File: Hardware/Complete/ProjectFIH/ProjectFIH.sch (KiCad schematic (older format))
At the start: 84 parts, among them J1 Conn_01x02_Male, J10 Payload LED, J2 Power, J3 Power LED, J4 MCU Fail LED, J5 Heater LED, J6 Heater, J7 UART, J8 AVR-ISP-10, J9 Payload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

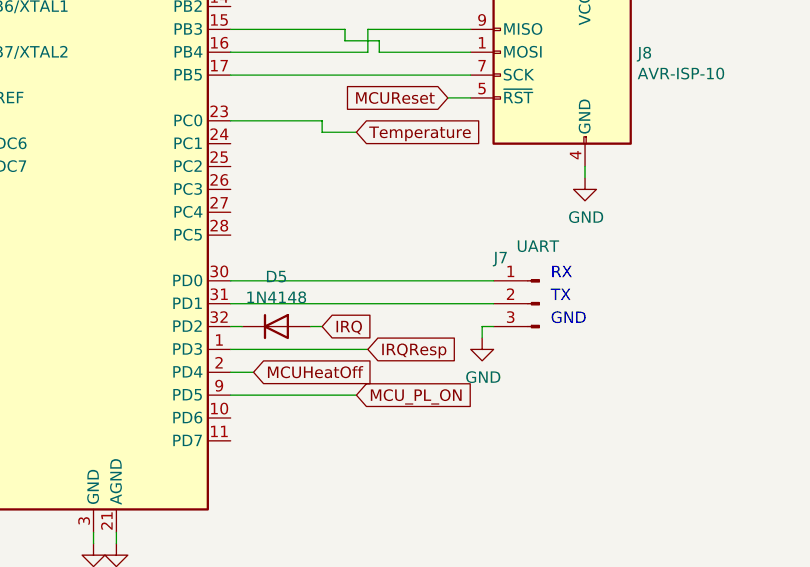
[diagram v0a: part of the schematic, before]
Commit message: MCU coupled with hardware watchdog
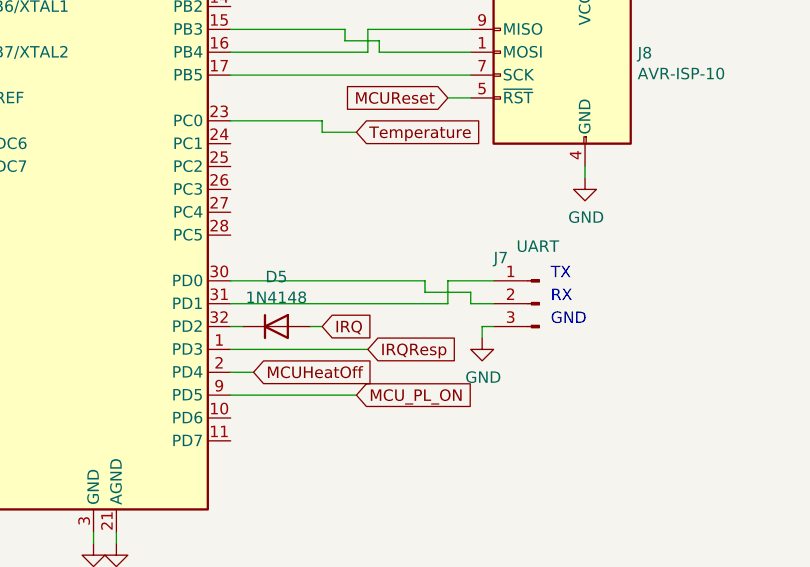
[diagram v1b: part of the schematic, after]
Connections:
- net at U8.30 (PD0): now also J7.2 (Pin_2); no longer J7.1 (Pin_1)
- net at U8.31 (PD1): now also J7.1 (Pin_1); no longer J7.2 (Pin_2)
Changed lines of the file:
@@
 	-1   0    0    -1
 $EndComp
-Wire Wire Line
-	12300 6450 11150 6450
-Wire Wire Line
-	12300 6550 11150 6550
 $Comp
 L power:GND #PWR059
@@
 Wire Wire Line
 	12250 6650 12250 6700
+Text Notes 12550 6550 0    50   ~ 0
+RX
 Text Notes 12550 6450 0    50   ~ 0
-RX
-Text Notes 12550 6550 0    50   ~ 0
 TX
 Text Notes 12550 6650 0    50   ~ 0
@@
 	8200 2400 8200 2550
 Connection ~ 8200 2550
+Wire Wire Line
+	11150 6550 12100 6550
+Wire Wire Line
+	12100 6550 12100 6450
+Wire Wire Line
+	12100 6450 12300 6450
+Wire Wire Line
+	12300 6550 12200 6550
+Wire Wire Line
+	12200 6550 12200 6500
+Wire Wire Line
+	12200 6500 12000 6500
+Wire Wire Line
+	12000 6500 12000 6450
+Wire Wire Line
+	12000 6450 11150 6450
 $EndSCHEMATC

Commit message: Small corrections after laying IRL parts out
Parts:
- C13, C14, C9: footprint Capacitor_THT:CP_Radial_D12.5mm_P7.50mm -> Capacitor_THT:CP_Radial_D12.5mm_P5.00mm
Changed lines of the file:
@@
 F 0 "C13" H 8850 1500 50  0000 L CNN
 F 1 "1000uF x 48V" H 8550 1300 50  0000 L CNN
-F 2 "Capacitor_THT:CP_Radial_D12.5mm_P7.50mm" H 8888 1250 50  0001 C CNN
+F 2 "Capacitor_THT:CP_Radial_D12.5mm_P5.00mm" H 8888 1250 50  0001 C CNN
 F 3 "~" H 8850 1400 50  0001 C CNN
 	1    8850 1400
@@
 F 0 "C14" H 8850 3100 50  0000 L CNN
 F 1 "1000uF x 48V" H 8550 2900 50  0000 L CNN
-F 2 "Capacitor_THT:CP_Radial_D12.5mm_P7.50mm" H 8888 2850 50  0001 C CNN
+F 2 "Capacitor_THT:CP_Radial_D12.5mm_P5.00mm" H 8888 2850 50  0001 C CNN
 F 3 "~" H 8850 3000 50  0001 C CNN
 	1    8850 3000
@@
 F 0 "C9" H 4218 9596 50  0000 L CNN
 F 1 "1000uFx50V" H 4218 9505 50  0000 L CNN
-F 2 "Capacitor_THT:CP_Radial_D12.5mm_P7.50mm" H 4138 9400 50  0001 C CNN
+F 2 "Capacitor_THT:CP_Radial_D12.5mm_P5.00mm" H 4138 9400 50  0001 C CNN
 F 3 "~" H 4100 9550 50  0001 C CNN
 	1    4100 9550

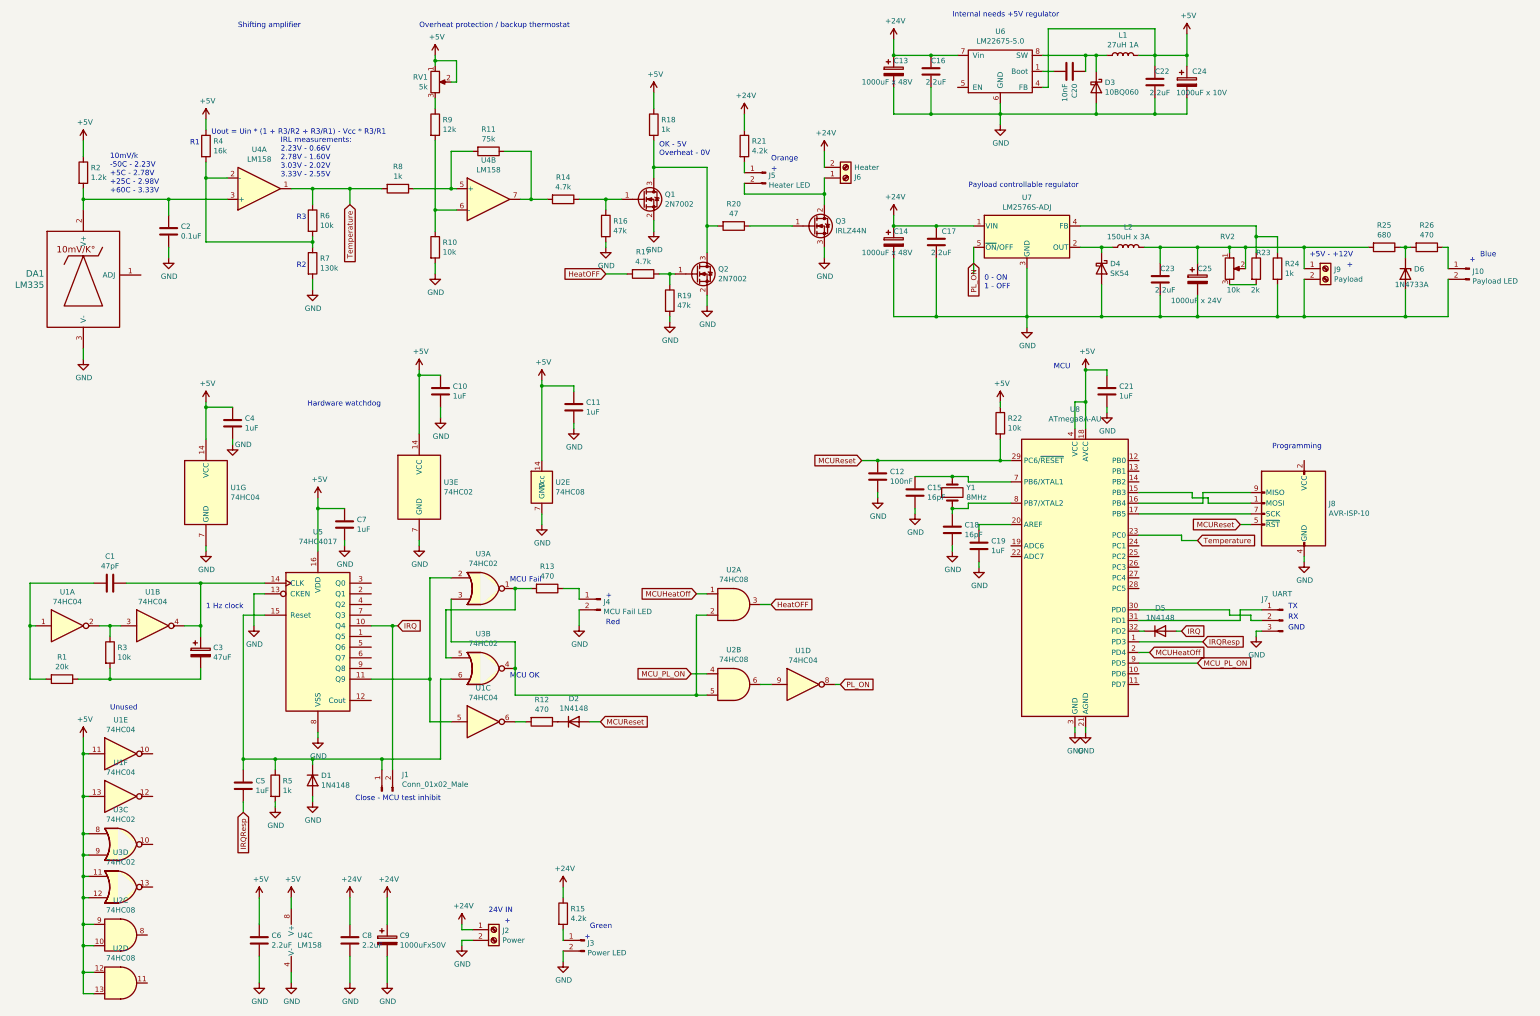
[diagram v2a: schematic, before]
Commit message: Flipped some (but not all needed) parts to other side
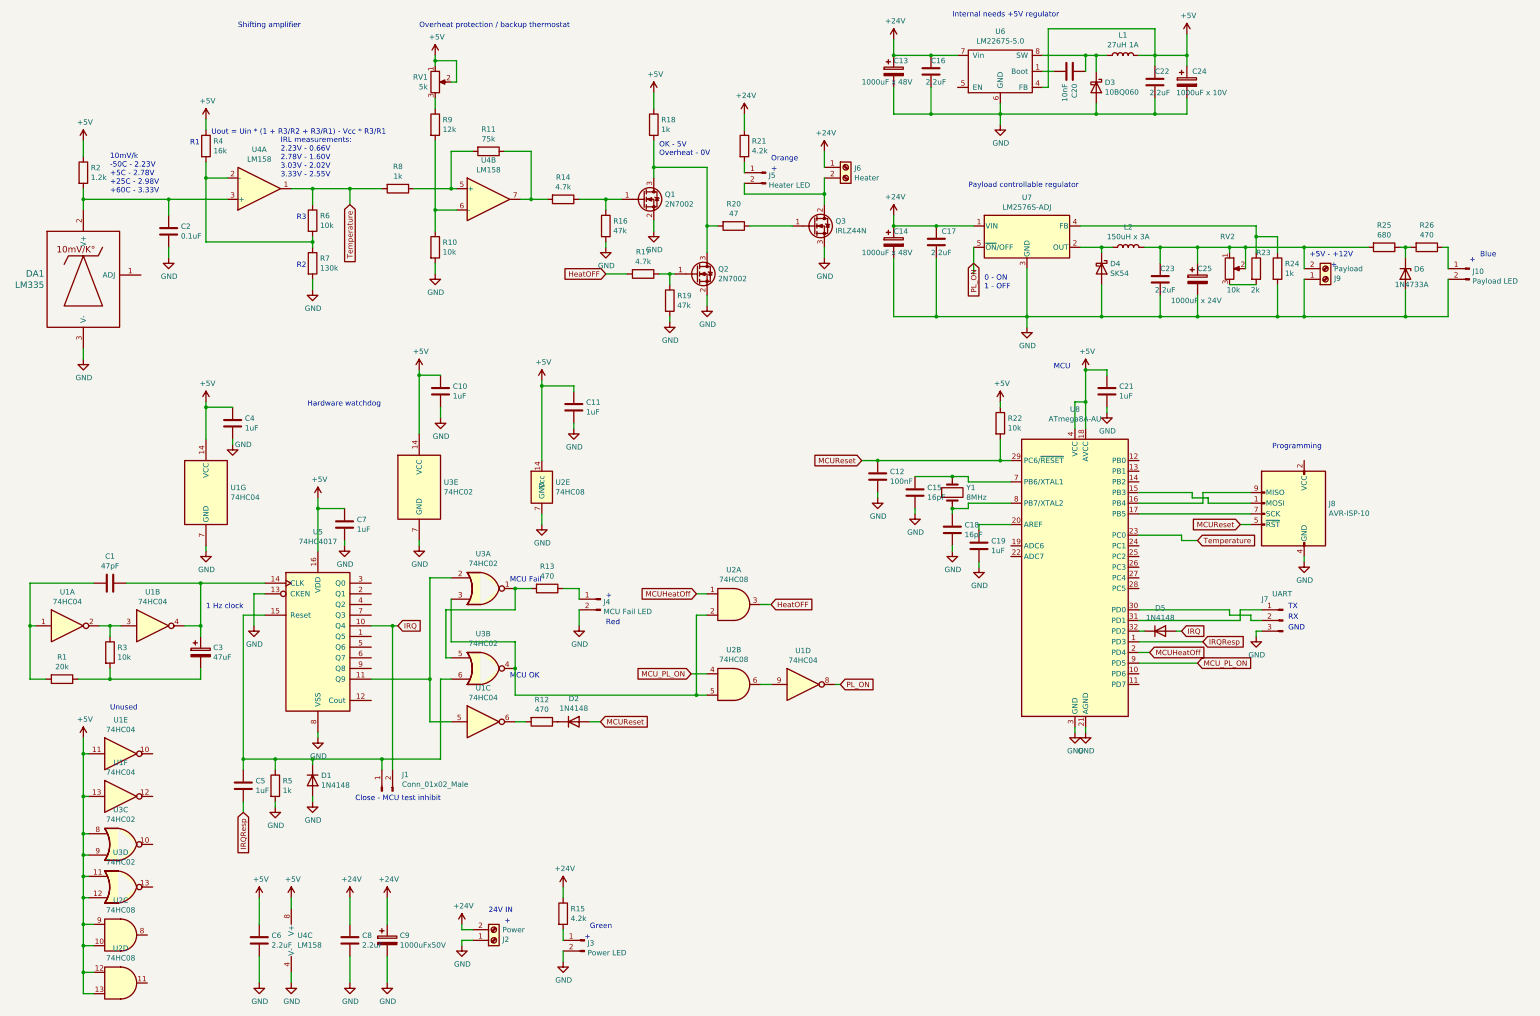
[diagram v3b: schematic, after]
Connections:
- net +24V: now also J2.2 (Pin_2), J6.1 (Pin_1); no longer J2.1 (Pin_1), J6.2 (Pin_2)
- net GND: now also J2.1 (Pin_1), J9.1 (Pin_1); no longer J2.2 (Pin_2), J9.2 (Pin_2)
- net at J5.2 (Pin_2), Q3.2 (D): now also J6.2 (Pin_2); no longer J6.1 (Pin_1)
- net at C23.1, C25.1, L2.2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: now also J9.2 (Pin_2); no longer J9.1 (Pin_1)
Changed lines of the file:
@@
 L Connector:Screw_Terminal_01x02 J6
 U 1 1 5F039ABC
-P 8400 2400
-F 0 "J6" H 8480 2392 50  0000 L CNN
-F 1 "Heater" H 8480 2301 50  0000 L CNN
-F 2 "TerminalBlock:TerminalBlock_Altech_AK300-2_P5.00mm" H 8400 2400 50  0001 C CNN
-F 3 "~" H 8400 2400 50  0001 C CNN
-	1    8400 2400
-	1    0    0    1
+P 8400 2300
+F 0 "J6" H 8480 2292 50  0000 L CNN
+F 1 "Heater" H 8480 2201 50  0000 L CNN
+F 2 "TerminalBlock:TerminalBlock_Altech_AK300-2_P5.00mm" H 8400 2300 50  0001 C CNN
+F 3 "~" H 8400 2300 50  0001 C CNN
+	1    8400 2300
+	1    0    0    -1
 $EndComp
 $Comp
@@
 L Connector:Screw_Terminal_01x02 J9
 U 1 1 5F15006B
-P 12900 3250
-F 0 "J9" H 12980 3242 50  0000 L CNN
-F 1 "Payload" H 12980 3151 50  0000 L CNN
-F 2 "TerminalBlock:TerminalBlock_Altech_AK300-2_P5.00mm" H 12900 3250 50  0001 C CNN
-F 3 "~" H 12900 3250 50  0001 C CNN
-	1    12900 3250
-	1    0    0    -1
+P 12900 3350
+F 0 "J9" H 12980 3342 50  0000 L CNN
+F 1 "Payload" H 12980 3251 50  0000 L CNN
+F 2 "TerminalBlock:TerminalBlock_Altech_AK300-2_P5.00mm" H 12900 3350 50  0001 C CNN
+F 3 "~" H 12900 3350 50  0001 C CNN
+	1    12900 3350
+	1    0    0    1
 $EndComp
 Wire Wire Line
@@
 L Connector:Screw_Terminal_01x02 J2
 U 1 1 5F880536
-P 5100 9450
-F 0 "J2" H 5180 9442 50  0000 L CNN
-F 1 "Power" H 5180 9351 50  0000 L CNN
-F 2 "TerminalBlock:TerminalBlock_Altech_AK300-2_P5.00mm" H 5100 9450 50  0001 C CNN
-F 3 "~" H 5100 9450 50  0001 C CNN
-	1    5100 9450
-	1    0    0    -1
+P 5100 9550
+F 0 "J2" H 5180 9542 50  0000 L CNN
+F 1 "Power" H 5180 9451 50  0000 L CNN
+F 2 "TerminalBlock:TerminalBlock_Altech_AK300-2_P5.00mm" H 5100 9550 50  0001 C CNN
+F 3 "~" H 5100 9550 50  0001 C CNN
+	1    5100 9550
+	1    0    0    1
 $EndComp
 $Comp
@@
 Text Notes 5200 9400 0    50   ~ 0
 +
-Text Notes 13100 3250 0    50   ~ 0
+Text Notes 12950 3250 0    50   ~ 0
 +
 $Comp

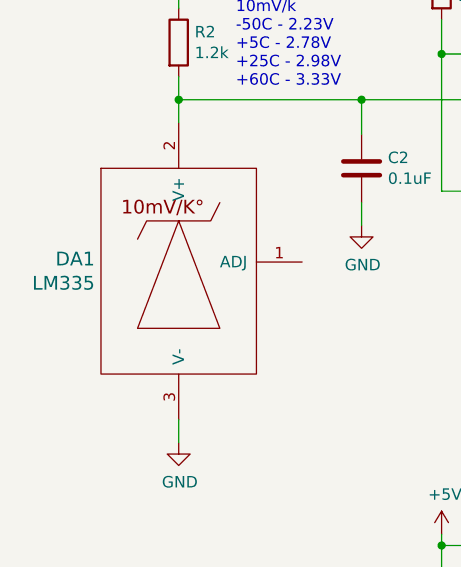
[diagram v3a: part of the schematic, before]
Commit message: LM335 -> LM135
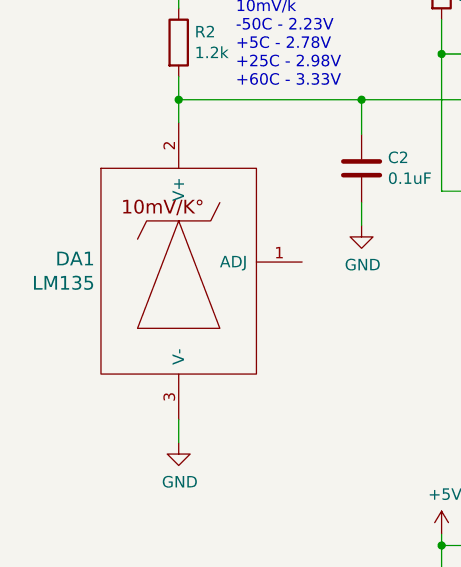
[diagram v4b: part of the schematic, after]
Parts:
- DA1: value LM335 -> LM135
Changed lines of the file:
@@
 P 1250 2900
 F 0 "DA1" H 883 2503 60  0000 R CNN
-F 1 "LM335" H 883 2397 60  0000 R CNN
+F 1 "LM135" H 883 2397 60  0000 R CNN
 F 2 "Package_TO_SOT_THT:TO-92" H 1240 2910 60  0001 C CNN
 F 3 "" H 1240 2910 60  0000 C CNN

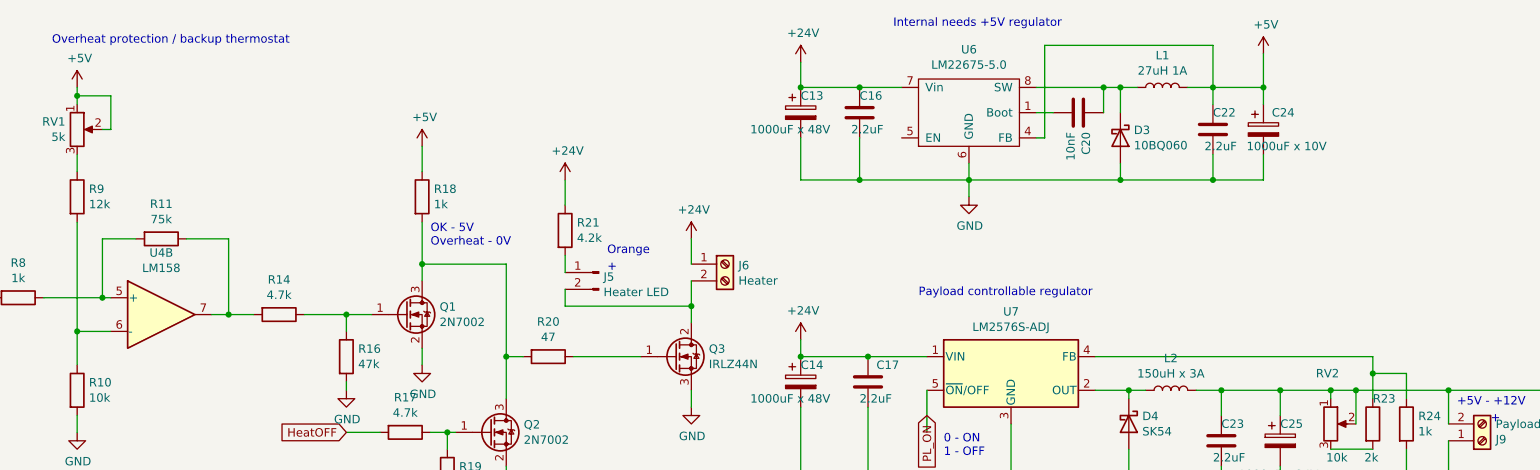
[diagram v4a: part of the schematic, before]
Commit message: Small comments on schematic
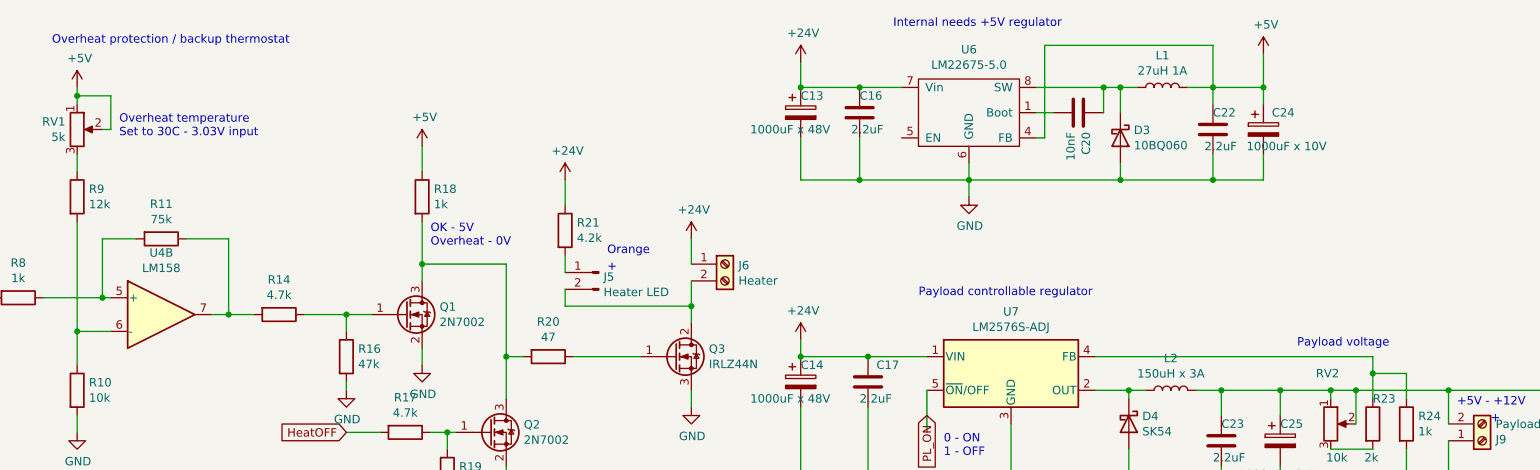
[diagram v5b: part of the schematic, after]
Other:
- note added: "Overheat temperature\nSet to 30C - 3.03V input"
- note added: "Payload voltage"
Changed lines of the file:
@@
 Wire Wire Line
 	12000 6450 11150 6450
+Text Notes 11800 2800 0    50   ~ 0
+Payload voltage
+Text Notes 4800 1550 0    50   ~ 0
+Overheat temperature\nSet to 30C - 3.03V input
 $EndSCHEMATC

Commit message: Small corrections
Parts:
- added R27: 470, Resistor_SMD:R_0805_2012Metric_Pad1.15x1.40mm_HandSolder, symbol Device:R
- R15, R21: value 4.2k -> 4.3k
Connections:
- net IRQ: now also R27.1; no longer D5.2 (A)
- new net: D5.2 (A), R27.2
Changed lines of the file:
@@
 Text Notes 12400 4950 0    50   ~ 0
 Programming
-Text GLabel 11550 6650 2    50   Input ~ 0
+Text GLabel 11950 6850 2    50   Input ~ 0
 IRQ
 $Comp
@@
 Wire Wire Line
 	11200 6650 11150 6650
-Wire Wire Line
-	11550 6650 11500 6650
-Text GLabel 11750 6750 2    50   Input ~ 0
+Text GLabel 11800 6950 2    50   Input ~ 0
 IRQResp
-Wire Wire Line
-	11750 6750 11150 6750
-Text GLabel 11250 6850 2    50   Input ~ 0
+Text GLabel 11700 7050 2    50   Input ~ 0
 MCUHeatOff
-Wire Wire Line
-	11250 6850 11150 6850
-Text GLabel 11700 6950 2    50   Input ~ 0
+Text GLabel 11700 7150 2    50   Input ~ 0
 MCU_PL_ON
-Wire Wire Line
-	11700 6950 11150 6950
 Text GLabel 3750 2650 3    50   Input ~ 0
 Temperature
@@
 P 5750 9300
 F 0 "R15" H 5820 9346 50  0000 L CNN
-F 1 "4.2k" H 5820 9255 50  0000 L CNN
+F 1 "4.3k" H 5820 9255 50  0000 L CNN
 F 2 "Resistor_SMD:R_0805_2012Metric_Pad1.15x1.40mm_HandSolder" V 5680 9300 50  0001 C CNN
 F 3 "~" H 5750 9300 50  0001 C CNN
@@
 P 7450 2100
 F 0 "R21" H 7520 2146 50  0000 L CNN
-F 1 "4.2k" H 7520 2055 50  0000 L CNN
+F 1 "4.3k" H 7520 2055 50  0000 L CNN
 F 2 "Resistor_SMD:R_0805_2012Metric_Pad1.15x1.40mm_HandSolder" V 7380 2100 50  0001 C CNN
 F 3 "~" H 7450 2100 50  0001 C CNN
@@
 Text Notes 4800 1550 0    50   ~ 0
 Overheat temperature\nSet to 30C - 3.03V input
+Wire Wire Line
+	11150 6950 11250 6950
+Wire Wire Line
+	11250 6950 11250 7150
+Wire Wire Line
+	11250 7150 11700 7150
+Wire Wire Line
+	11300 6850 11300 7050
+Wire Wire Line
+	11300 7050 11700 7050
+Wire Wire Line
+	11150 6850 11300 6850
+Wire Wire Line
+	11350 6950 11350 6750
+Wire Wire Line
+	11350 6750 11150 6750
+Wire Wire Line
+	11350 6950 11800 6950
+$Comp
+L Device:R R27
+U 1 1 5F536347
+P 11700 6850
+F 0 "R27" V 11493 6850 50  0000 C CNN
+F 1 "470" V 11584 6850 50  0000 C CNN
+F 2 "Resistor_SMD:R_0805_2012Metric_Pad1.15x1.40mm_HandSolder" V 11630 6850 50  0001 C CNN
+F 3 "~" H 11700 6850 50  0001 C CNN
+	1    11700 6850
+	0    1    1    0
+$EndComp
+Wire Wire Line
+	11950 6850 11850 6850
+Wire Wire Line
+	11550 6850 11550 6650
+Wire Wire Line
+	11550 6650 11500 6650
 $EndSCHEMATC
